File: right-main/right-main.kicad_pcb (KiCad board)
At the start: 2 copper layers, 150.1 x 123.4 mm, 285 parts, among them J1 548190519, P1 A-2004-3-4-LP-N-R, P2 CONN_5, P3 3220-10-0100-00, P4 CONN_6, P5 CONN_6, Q1 MOSFET_N, SW1 CT05-3050-G1, SW11 7, SW12 8, SW13 9, SW14 0, SW15 -, SW16 =, SW17 BACKSPACE, SW2 EVQPLMA15, SW21 U, SW22 I, SW23 O, SW24 P, SW25 [, SW26 ], SW27 \, SW31 Y, SW32 J, SW33 K, SW34 L, SW35 ;, SW36 ', SW37 ENTER, SW41 H, SW42 N, SW43 M, SW44 ,, SW45 ., SW46 /, SW47 R_SHIFT, SW52 R_SPACE, SW53 R_MOD, SW54 R_FN, SW55 R_ALT, SW56 R_SUPER, SW57 R_CTRL, U1 MK22FN512VLH12, U2 CAT24C256WI-GT3, U3 IS31FL3731, U5 ESD, U6 ESD, U7 ESD

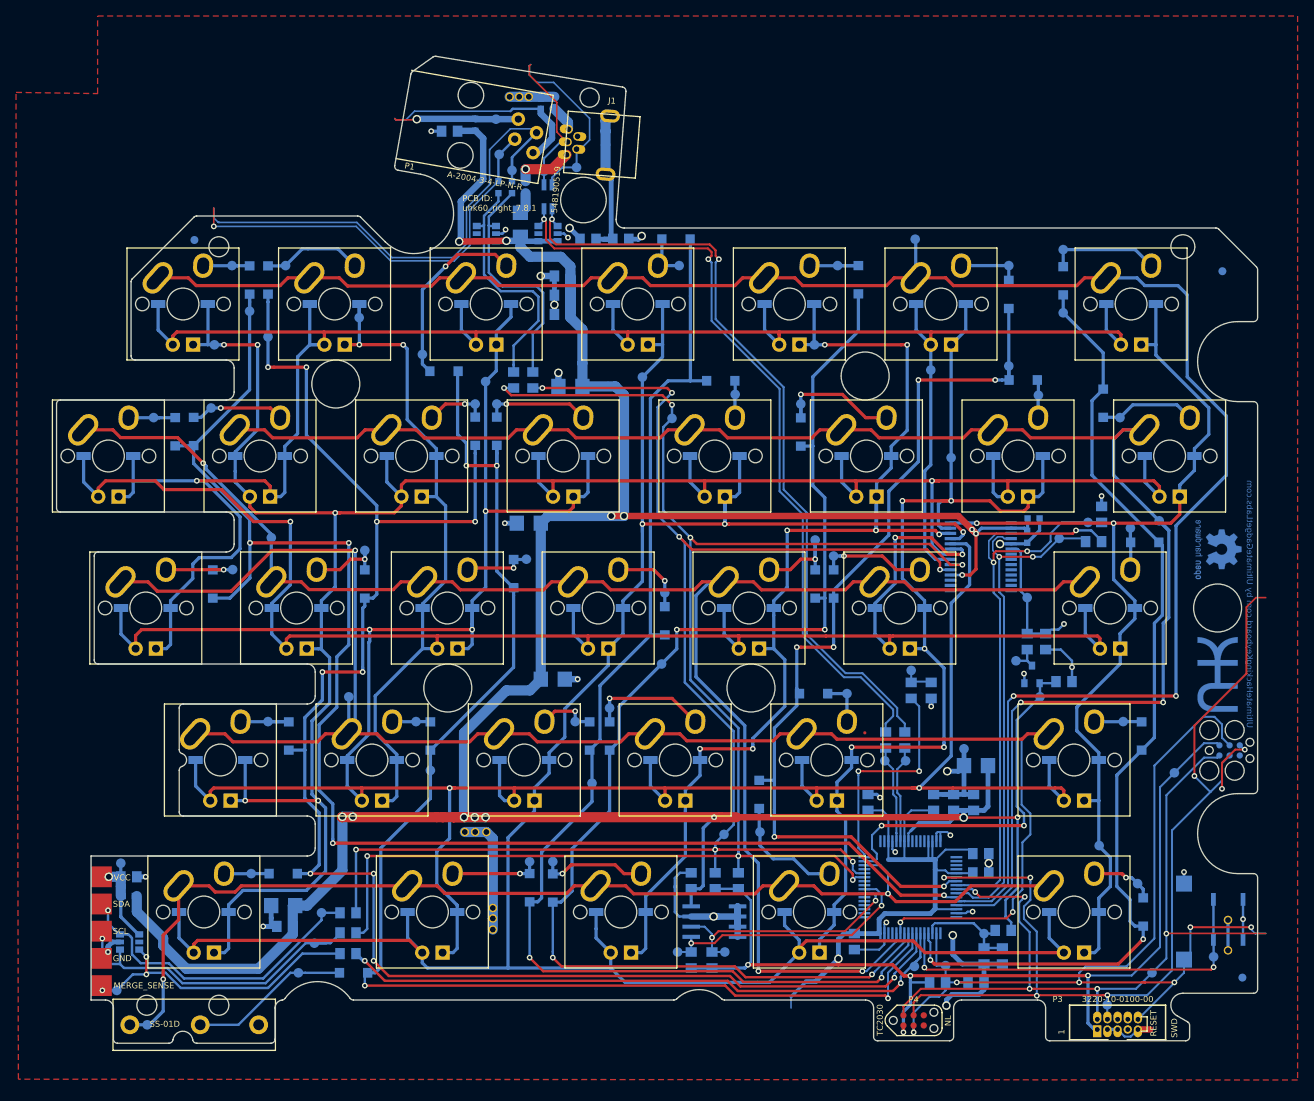
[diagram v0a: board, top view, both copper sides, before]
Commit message: Right switches changed to Choc, relayout mostly complete
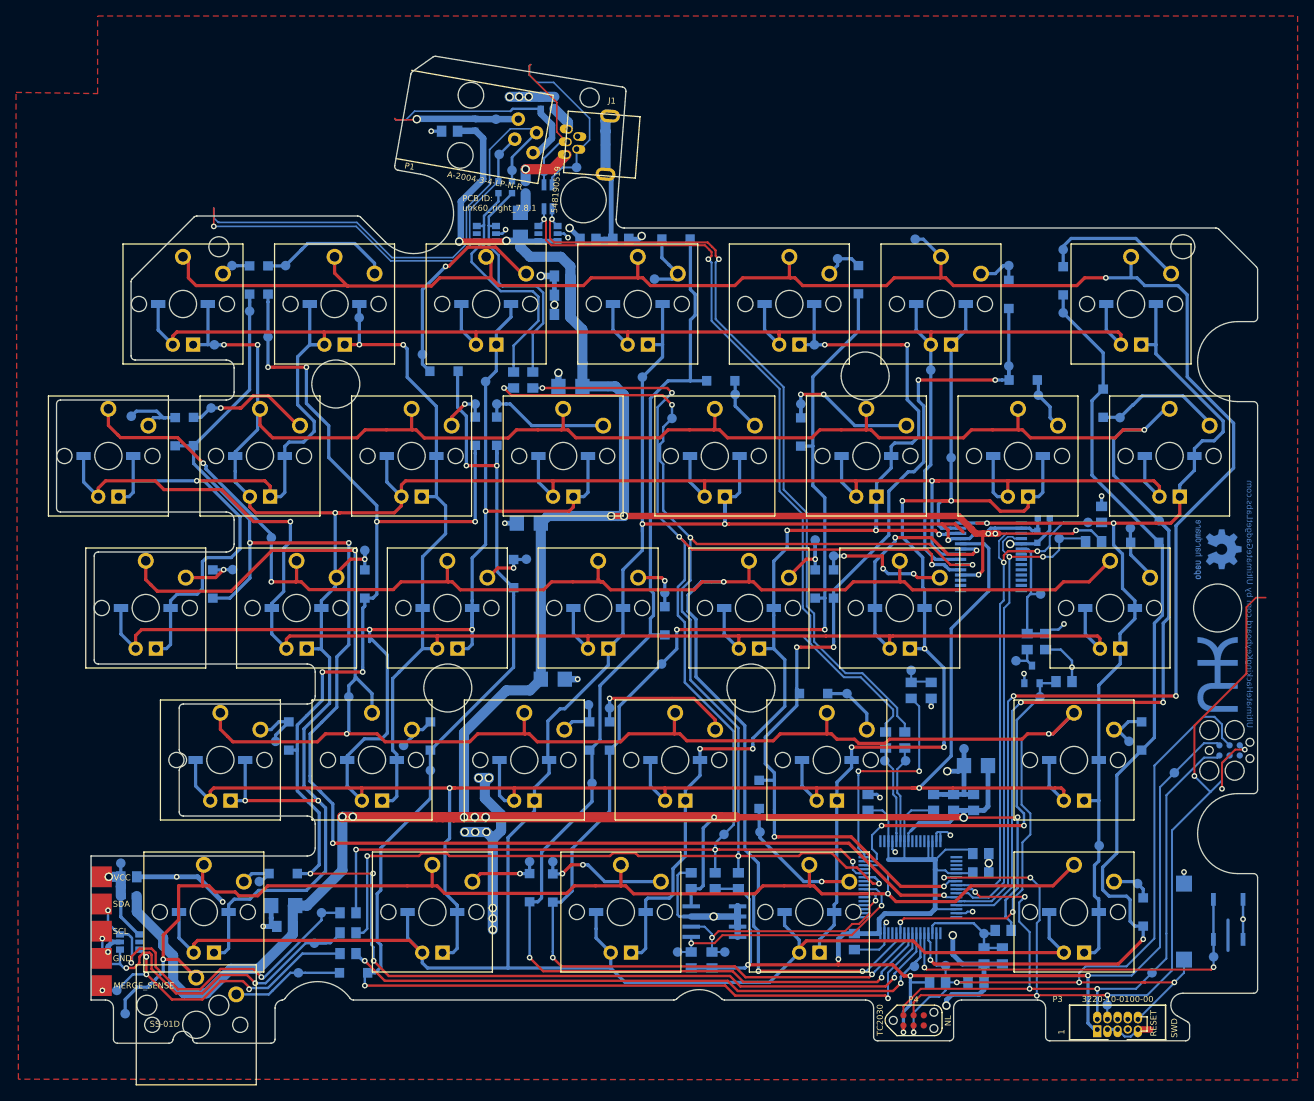
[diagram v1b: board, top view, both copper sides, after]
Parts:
- removed FID1, FID2, FID3: >VALUE, Input_Club:FID
- removed GndVia1, GndVia2, GndVia3, GndVia4, GndVia5, GndVia6, GndVia7, GndVia8, GndVia9: VIA, UGL:via_28_42mil_solid_con
- removed VIA1, VIA2: via_28_42mil_solid_con, UGL:via_28_42mil_solid_con
- SW11, SW12, SW13, SW14, SW15, SW16, SW17, SW21, SW22, SW23, SW24, SW25, SW26, SW27, SW31, SW32, SW33, SW34, SW35, SW36, SW37, SW41, SW43, SW44, SW45, SW46, SW47, SW52, SW54, SW55, SW56, SW57: footprint UGL:Cherry_MX_Matias_Hybrid -> Borgel Custom:CPG135001D02
- SW42: footprint UGL:Cherry_MX_Matias_Hybrid_Right_Pin -> Borgel Custom:CPG135001D02
- SW53: footprint UGL:SS-01D -> Borgel Custom:CPG135001D02
- moved TP_SW14_D1 3.52 mm to (196.2, 57.8)
- moved TP_SW43_D1 3.36 mm to (164.8, 116.1)
- moved TP_KEYS_ROW5 3.08 mm to (130.0, 149.6)
- moved TP_SW31_D1 2.80 mm to (130.8, 74.9)
- moved TP_SW44_D1 2.68 mm to (188.0, 111.0)
- moved TP_SW42_D1 2.64 mm to (148.8, 115.6)
- moved TP_SW47_D1 2.57 mm to (255.5, 115.6)
- moved TP_R_EXT1 1.73 mm to (244.5, 97.2)
- moved TP_SW52_D1 1.42 mm to (146.8, 133.1)
- moved C19 1.27 mm to (244.9, 87.7)
- moved U3 1.27 mm to (238.3, 92.5)
- moved C5 1.27 mm to (244.1, 90.0)
- moved TP_SW15_D1 0.86 mm to (219.1, 55.2)
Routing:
- net GND: track 163.4 -> 184.3 mm, vias 32 -> 44
- net /KEYS_ROW3: track 215.1 -> 233.8 mm, vias 3 -> 5
- net /KEYS_ROW5: track 139.9 -> 158.4 mm
- net /KEYS_ROW2: track 210.0 -> 226.7 mm, vias 2 -> 3
- net /KEYS_ROW4: track 212.7 -> 229.0 mm, vias 3 -> 5
- net /KEYS_ROW1: track 245.6 -> 261.6 mm, vias 2 -> 3
- net /RESET: track 120.3 -> 107.1 mm, vias 6 -> 4
- net /SWDIO: track 107.7 -> 95.2 mm, vias 5 -> 4
- net +3V3: track 197.8 -> 188.5 mm
- net /SCL: track 197.5 -> 204.7 mm
- net /SW53_D: track 20.1 -> 14.0 mm
- net /SDA_BOTTOM: track 38.6 -> 44.4 mm, vias 1 -> 3
- net /CA6: track 136.8 -> 142.1 mm
- net /CA1: track 280.9 -> 285.8 mm
- net /SCL_BOTTOM: track 39.6 -> 44.6 mm, vias 1 -> 3
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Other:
- net class Default: clearance 0 -> 0.1524
- rule trace_clearance: 0 -> 0.1524

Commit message: Finish integrating Choc into right side
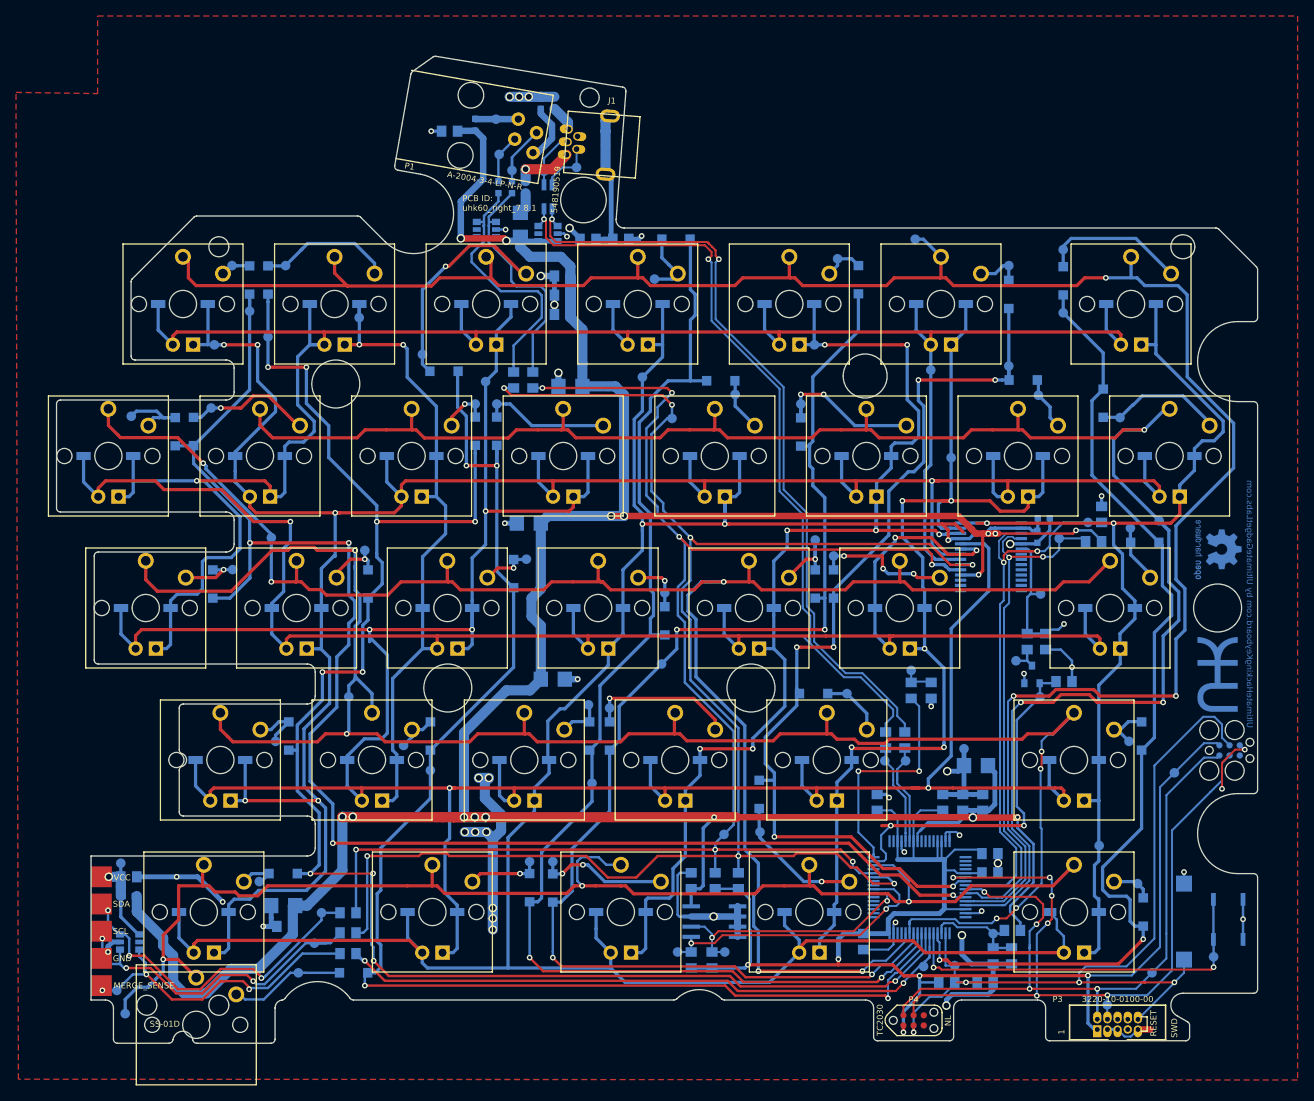
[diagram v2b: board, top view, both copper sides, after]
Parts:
- hole: footprint UGL:hole_6mm -> UGL:hole_5.5mm
- moved C14 1.14 mm to (224.0, 123.2)
- moved C15 1.14 mm to (234.7, 123.2)
- moved C16 1.14 mm to (237.2, 123.2)
- moved C3 1.14 mm to (222.3, 140.6)
- moved C32 1.14 mm to (238.1, 129.6)
- moved C33 1.14 mm to (232.2, 123.2)
- moved C34 1.14 mm to (238.5, 142.4)
- moved C4 1.14 mm to (238.1, 132.0)
- moved C7 1.14 mm to (237.5, 145.7)
- moved R1 1.14 mm to (232.7, 145.7)
- moved R10 1.14 mm to (240.9, 139.2)
- moved R19 1.14 mm to (240.8, 142.4)
- moved TP_ADC1 1.14 mm to (238.5, 139.6)
- moved TP_MERGE_SENSE1 1.14 mm to (229.8, 143.7)
- moved TP_RESET1 1.14 mm to (233.7, 143.6)
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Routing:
- net /SDA_TOP: track 64.7 -> 8.99 mm
- net /SCL_TOP: track 52.5 -> 6.14 mm, vias 1 -> 0
- net /SWDCLK: track 126.9 -> 99.0 mm, vias 5 -> 6
- net /GND_TOP: track 26.3 -> 7.40 mm
- net /USB_D_IN-: track 22.9 -> 6.94 mm
- net /USB_D_IN+: track 20.6 -> 8.83 mm
- net /VCC_TOP: track 18.2 -> 8.03 mm, vias 1 -> 0
- net /KEYS_ROW5: track 158.4 -> 167.1 mm, vias 2 -> 3
- net /SCL: track 204.7 -> 210.3 mm
- net /KEYS_ROW2: track 226.7 -> 230.2 mm
- net /SDA2: track 35.0 -> 38.3 mm
- net /KEYS_ROW1: track 261.6 -> 264.7 mm
- net /SDA_BOTTOM: track 44.4 -> 41.4 mm
- net /SDB: track 71.0 -> 73.9 mm
- net /SCL_BOTTOM: track 44.6 -> 41.7 mm
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
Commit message: Playing with movement of switches
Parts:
- added SW17: BACKSPACE, Borgel Custom:CPG135001D02, F.Cu at (255.8, 137.2)
- added SW27: \, Borgel Custom:CPG135001D02, F.Cu at (260.5, 137.0)
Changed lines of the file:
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@@
     (tracks 2571)
     (zones 0)
-    (modules 271)
+    (modules 273)
     (nets 135)
   )
@@
   )
   (layers
-    (0 F.Cu signal)
-    (31 B.Cu signal)
+    (0 F.Cu signal hide)
+    (31 B.Cu signal hide)
     (34 B.Paste user)
     (35 F.Paste user)
@@
     (add_net "Net-(U3-Pad9)")
   )
+  (module "Borgel Custom:CPG135001D02" locked (layer F.Cu)
+    (at 255.785007 137.16)
+    (fp_text reference SW17 (at 5.08 -6.35) (layer B.SilkS)
+      (effects (font (size 1 1) (thickness 0.15)) (justify mirror))
+    )
+    (fp_text value BACKSPACE (at 0 8.255) (layer F.Fab)
+      (effects (font (size 1 1) (thickness 0.15)))
+    )
+    (fp_line (start -2.54 3.175) (end -2.54 6.35) (layer F.Fab) (width 0.12))
+    (fp_line (start -2.54 6.35) (end 2.54 6.35) (layer F.Fab) (width 0.12))
+    (fp_line (start 2.54 6.35) (end 2.54 3.175) (layer F.Fab) (width 0.12))
+    (fp_line (start 2.54 3.175) (end -2.54 3.175) (layer F.Fab) (width 0.12))
+    (fp_line (start -7.5 -7.5) (end 7.5 -7.5) (layer F.SilkS) (width 0.15))
+    (fp_line (start 7.5 -7.5) (end 7.5 7.5) (layer F.SilkS) (width 0.15))
+    (fp_line (start 7.5 7.5) (end -7.5 7.5) (layer F.SilkS) (width 0.15))
+    (fp_line (start -7.5 7.5) (end -7.5 -7.5) (layer F.SilkS) (width 0.15))
+    (pad "" np_thru_hole circle (at 0 0) (size 3.4 3.4) (drill 3.4) (layers *.Cu *.Mask))
+    (pad 1 thru_hole circle (at 0 -5.9) (size 2 2) (drill 1.2) (layers *.Cu *.Mask)
+      (net 31 /KEYS_ROW1))
+    (pad 2 thru_hole circle (at 5 -3.8) (size 2 2) (drill 1.2) (layers *.Cu *.Mask)
+      (net 89 /SW17_D))
+    (pad "" np_thru_hole circle (at 5.5 0) (size 1.9 1.9) (drill 1.9) (layers *.Cu *.Mask))
+    (pad "" np_thru_hole circle (at -5.5 0) (size 1.9 1.9) (drill 1.9) (layers *.Cu *.Mask))
+  )
+  (module "Borgel Custom:CPG135001D02" locked (layer F.Cu)
+    (at 260.5405 136.9695)
+    (fp_text reference SW27 (at 5.08 -6.35) (layer B.SilkS)
+      (effects (font (size 1 1) (thickness 0.15)) (justify mirror))
+    )
+    (fp_text value \ (at 0 8.255) (layer F.Fab)
+      (effects (font (size 1 1) (thickness 0.15)))
+    )
+    (fp_line (start -2.54 3.175) (end -2.54 6.35) (layer F.Fab) (width 0.12))
+    (fp_line (start -2.54 6.35) (end 2.54 6.35) (layer F.Fab) (width 0.12))
+    (fp_line (start 2.54 6.35) (end 2.54 3.175) (layer F.Fab) (width 0.12))
+    (fp_line (start 2.54 3.175) (end -2.54 3.175) (layer F.Fab) (width 0.12))
+    (fp_line (start -7.5 -7.5) (end 7.5 -7.5) (layer F.SilkS) (width 0.15))
+    (fp_line (start 7.5 -7.5) (end 7.5 7.5) (layer F.SilkS) (width 0.15))
+    (fp_line (start 7.5 7.5) (end -7.5 7.5) (layer F.SilkS) (width 0.15))
+    (fp_line (start -7.5 7.5) (end -7.5 -7.5) (layer F.SilkS) (width 0.15))
+    (pad "" np_thru_hole circle (at 0 0) (size 3.4 3.4) (drill 3.4) (layers *.Cu *.Mask))
+    (pad 1 thru_hole circle (at 0 -5.9) (size 2 2) (drill 1.2) (layers *.Cu *.Mask)
+      (net 32 /KEYS_ROW2))
+    (pad 2 thru_hole circle (at 5 -3.8) (size 2 2) (drill 1.2) (layers *.Cu *.Mask)
+      (net 96 /SW27_D))
+    (pad "" np_thru_hole circle (at 5.5 0) (size 1.9 1.9) (drill 1.9) (layers *.Cu *.Mask))
+    (pad "" np_thru_hole circle (at -5.5 0) (size 1.9 1.9) (drill 1.9) (layers *.Cu *.Mask))
+  )
   (module UGL:hole_5.5mm locked (layer F.Cu)
